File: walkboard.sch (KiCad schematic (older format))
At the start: 9 parts

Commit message: finished microcontroller
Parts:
- added C? (x2): 22pF, symbol Device:C_Small
- added F?: 500mA, symbol Device:Polyfuse_Small
- added J?: USB_C_Receptacle_USB2.0, symbol Connector:USB_C_Receptacle_USB2.0
- added R?: 10k, symbol Device:R_Small
- added SW?: SW_Push, symbol Switch:SW_Push
- added Y?: Crystal_GND24_Small, symbol Device:Crystal_GND24_Small
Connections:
- net labels added: D+, D-, VCC
- wire segments 25 -> 68

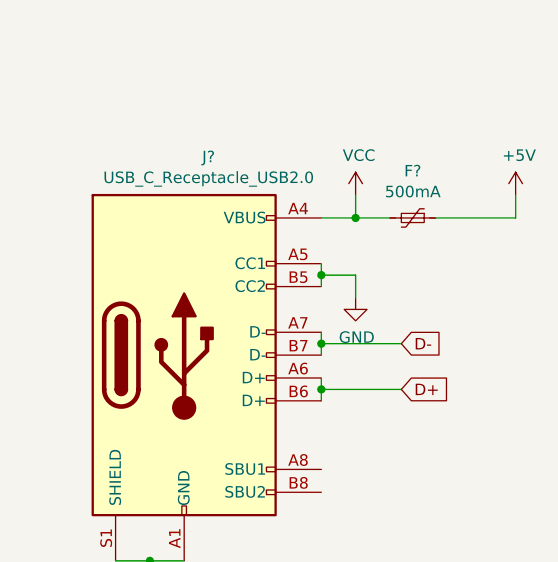
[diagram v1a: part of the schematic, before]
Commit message: added submodule for kaihl
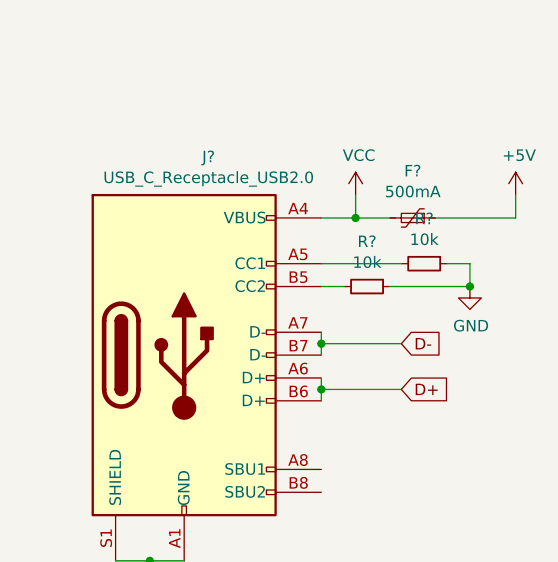
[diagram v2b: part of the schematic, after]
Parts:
- added R? (x2): 10k, symbol Device:R_Small
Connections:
- net GND: now also R?.1, R?.1; no longer J?.A5 (CC1), J?.B5 (CC2)
- new net: J?.B5 (CC2), R?.2
- new net: J?.A5 (CC1), R?.2
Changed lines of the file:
@@
 Text GLabel 7500 2100 2    50   Input ~ 0
 D-
-$Comp
-L power:GND #PWR?
-U 1 1 5F2C7BBD
-P 7300 1900
-F 0 "#PWR?" H 7300 1650 50  0001 C CNN
-F 1 "GND" H 7305 1727 50  0000 C CNN
-F 2 "" H 7300 1900 50  0001 C CNN
-F 3 "" H 7300 1900 50  0001 C CNN
-	1    7300 1900
-	1    0    0    -1
-$EndComp
-Wire Wire Line
-	7150 1750 7150 1800
-Wire Wire Line
-	7150 1800 7300 1800
-Wire Wire Line
-	7300 1800 7300 1900
-Connection ~ 7150 1800
-Wire Wire Line
-	7150 1800 7150 1850
 Wire Wire Line
 	7150 1550 7300 1550
@@
 Wire Wire Line
 	6400 3050 6550 3050
+$Comp
+L Device:R_Small R?
+U 1 1 5F2A1C28
+P 7350 1850
+F 0 "R?" V 7154 1850 50  0000 C CNN
+F 1 "10k" V 7245 1850 50  0000 C CNN
+F 2 "" H 7350 1850 50  0001 C CNN
+F 3 "~" H 7350 1850 50  0001 C CNN
+	1    7350 1850
+	0    1    1    0
+$EndComp
+$Comp
+L Device:R_Small R?
+U 1 1 5F2A2739
+P 7600 1750
+F 0 "R?" V 7404 1750 50  0000 C CNN
+F 1 "10k" V 7495 1750 50  0000 C CNN
+F 2 "" H 7600 1750 50  0001 C CNN
+F 3 "~" H 7600 1750 50  0001 C CNN
+	1    7600 1750
+	0    1    1    0
+$EndComp
+$Comp
+L power:GND #PWR?
+U 1 1 5F2A528D
+P 7800 1850
+F 0 "#PWR?" H 7800 1600 50  0001 C CNN
+F 1 "GND" H 7805 1677 50  0000 C CNN
+F 2 "" H 7800 1850 50  0001 C CNN
+F 3 "" H 7800 1850 50  0001 C CNN
+	1    7800 1850
+	1    0    0    -1
+$EndComp
+Wire Wire Line
+	7700 1750 7800 1750
+Wire Wire Line
+	7800 1750 7800 1850
+Wire Wire Line
+	7450 1850 7800 1850
+Connection ~ 7800 1850
+Wire Wire Line
+	7250 1850 7150 1850
+Wire Wire Line
+	7150 1750 7500 1750
 $EndSCHEMATC

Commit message: started work on pcb
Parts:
- removed R? (x2): 22, symbol Device:R_Small
- added D1, D10, D11, D12, D13, D14, D15, D16, D17, D18, D19, D2, D20, D21, D22, D23, D24, D25, D26, D27, D28, D29, D3, D30, D31, D32, D33, D34, D35, D36, D37, D38, D39, D4, D40, D41, D42, D43, D44, D45, D46, D47, D48, D49, D5, D50, D51, D52, D53, D54, D55, D56, D57, D58, D59, D6, D60, D61, D62, D63, D64, D65, D66, D67, D68, D7, D8, D9: D_Small, Diode_SMD:D_SOD-123, symbol Device:D_Small
- added MX1, MX10, MX11, MX12, MX13, MX14, MX15, MX16, MX17, MX18, MX19, MX2, MX20, MX21, MX22, MX23, MX24, MX25, MX26, MX27, MX28, MX29, MX3, MX30, MX31, MX32, MX33, MX34, MX35, MX36, MX37, MX38, MX39, MX4, MX40, MX41, MX42, MX43, MX44, MX45, MX46, MX47, MX48, MX49, MX5, MX50, MX51, MX52, MX53, MX54, MX55, MX56, MX57, MX58, MX59, MX6, MX60, MX61, MX62, MX63, MX64, MX65, MX66, MX67, MX7, MX8, MX9: MX-NoLED, keyswitches:Kailh_socket_MX, symbol MX_Alps_Hybrid:MX-NoLED
- added MX68: MX-NoLED, Resistor_SMD:R_0805_2012Metric, symbol MX_Alps_Hybrid:MX-NoLED
- added R2, R3: 22, Resistor_SMD:R_0612_1632Metric_Pad1.18x3.40mm_HandSolder, symbol Device:R_Small
- C1, C2, C3, C4, C5, C6: renamed from C?; footprint (none) -> Capacitor_SMD:C_0805_2012Metric_Pad1.15x1.40mm_HandSolder
- C7: renamed from C?; footprint (none) -> Diode_SMD:D_SOD-123
- F1: renamed from F?; footprint (none) -> keyswitches:Kailh_socket_MX
- J1: renamed from J?; footprint (none) -> Connector_USB:USB_C_Receptacle_HRO_TYPE-C-31-M-12
- R1, R4, R5, R6: renamed from R?; footprint (none) -> Resistor_SMD:R_0612_1632Metric_Pad1.18x3.40mm_HandSolder
- SW1: renamed from SW?; footprint (none) -> random-keyboard-parts:SKQG-1155865
- Y1: renamed from Y?; footprint (none) -> Crystal:Crystal_SMD_3225-4Pin_3.2x2.5mm
- gave numbers to parts that had none: 1
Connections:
- net D+: now also R2.2
- net D-: now also R3.2
- net at U1.3 (D-): now also R3.1
- net at U1.4 (D+): now also R2.1
- new net: D1.2 (A), MX1.2 (ROW)
- new net: D2.2 (A), MX2.2 (ROW)
- new net: D3.2 (A), MX3.2 (ROW)
- new net: D4.2 (A), MX4.2 (ROW)
- new net: D5.2 (A), MX5.2 (ROW)
- new net: D6.2 (A), MX6.2 (ROW)
- new net: D7.2 (A), MX7.2 (ROW)
- new net: D8.2 (A), MX8.2 (ROW)
- new net: D9.2 (A), MX9.2 (ROW)
- new net: D10.2 (A), MX10.2 (ROW)
- new net: D11.2 (A), MX11.2 (ROW)
- new net: D12.2 (A), MX12.2 (ROW)
- new net: D15.2 (A), MX15.2 (ROW)
- new net: D16.2 (A), MX16.2 (ROW)
- new net: D17.2 (A), MX17.2 (ROW)
- new net: D18.2 (A), MX18.2 (ROW)
- new net: D19.2 (A), MX19.2 (ROW)
- new net: D20.2 (A), MX20.2 (ROW)
- new net: D21.2 (A), MX21.2 (ROW)
- new net: D22.2 (A), MX22.2 (ROW)
- new net: D23.2 (A), MX23.2 (ROW)
- new net: D24.2 (A), MX24.2 (ROW)
- new net: D25.2 (A), MX25.2 (ROW)
- new net: D26.2 (A), MX26.2 (ROW)
- new net: D29.2 (A), MX29.2 (ROW)
- new net: D30.2 (A), MX30.2 (ROW)
- new net: D31.2 (A), MX31.2 (ROW)
- new net: D32.2 (A), MX32.2 (ROW)
- new net: D33.2 (A), MX33.2 (ROW)
- new net: D34.2 (A), MX34.2 (ROW)
- new net: D35.2 (A), MX35.2 (ROW)
- new net: D36.2 (A), MX36.2 (ROW)
- new net: D37.2 (A), MX37.2 (ROW)
- new net: D38.2 (A), MX38.2 (ROW)
- new net: D39.2 (A), MX39.2 (ROW)
- new net: D40.2 (A), MX40.2 (ROW)
- new net: D43.2 (A), MX43.2 (ROW)
- new net: D44.2 (A), MX44.2 (ROW)
- new net: D45.2 (A), MX45.2 (ROW)
- new net: D46.2 (A), MX46.2 (ROW)
- new net: D47.2 (A), MX47.2 (ROW)
- new net: D48.2 (A), MX48.2 (ROW)
- new net: D49.2 (A), MX49.2 (ROW)
- new net: D50.2 (A), MX50.2 (ROW)
- new net: D51.2 (A), MX51.2 (ROW)
- new net: D52.2 (A), MX52.2 (ROW)
- new net: D53.2 (A), MX53.2 (ROW)
- new net: D54.2 (A), MX54.2 (ROW)
- new net: D57.2 (A), MX57.2 (ROW)
- new net: D58.2 (A), MX58.2 (ROW)
- new net: D59.2 (A), MX59.2 (ROW)
- new net: D60.2 (A), MX60.2 (ROW)
- new net: D61.2 (A), MX61.2 (ROW)
- new net: D62.2 (A), MX62.2 (ROW)
- new net: D63.2 (A), MX63.2 (ROW)
- new net: D64.2 (A), MX64.2 (ROW)
- new net: D65.2 (A), MX65.2 (ROW)
- new net: D66.2 (A), MX66.2 (ROW)
- new net: D68.2 (A), MX68.2 (ROW)
- new net: D67.2 (A), MX67.2 (ROW)
- new net: D56.2 (A), MX56.2 (ROW)
- new net: D55.2 (A), MX55.2 (ROW)
- new net: D42.2 (A), MX42.2 (ROW)
- new net: D41.2 (A), MX41.2 (ROW)
- new net: D28.2 (A), MX28.2 (ROW)
- new net: D27.2 (A), MX27.2 (ROW)
- new net: D14.2 (A), MX14.2 (ROW)
- new net: D13.2 (A), MX13.2 (ROW)
- new net COL0: MX1.1 (COL), MX15.1 (COL), MX29.1 (COL), MX43.1 (COL), MX57.1 (COL)
- new net COL1: MX16.1 (COL), MX2.1 (COL), MX30.1 (COL), MX44.1 (COL), MX58.1 (COL)
- new net COL10: MX11.1 (COL), MX25.1 (COL), MX39.1 (COL), MX53.1 (COL), MX65.1 (COL)
- new net COL11: MX12.1 (COL), MX26.1 (COL), MX40.1 (COL), MX54.1 (COL), MX66.1 (COL)
- new net COL12: MX13.1 (COL), MX27.1 (COL), MX41.1 (COL), MX55.1 (COL), MX67.1 (COL)
- new net COL13: MX14.1 (COL), MX28.1 (COL), MX42.1 (COL), MX56.1 (COL), MX68.1 (COL)
- new net COL2: MX17.1 (COL), MX3.1 (COL), MX31.1 (COL), MX45.1 (COL), MX59.1 (COL)
- new net COL3: MX18.1 (COL), MX32.1 (COL), MX4.1 (COL), MX46.1 (COL), MX60.1 (COL)
- new net COL4: MX19.1 (COL), MX33.1 (COL), MX47.1 (COL), MX5.1 (COL), MX61.1 (COL)
- new net COL5: MX20.1 (COL), MX34.1 (COL), MX48.1 (COL), MX6.1 (COL), MX62.1 (COL)
- new net COL6: MX21.1 (COL), MX35.1 (COL), MX49.1 (COL), MX7.1 (COL)
- new net COL7: MX22.1 (COL), MX36.1 (COL), MX50.1 (COL), MX63.1 (COL), MX8.1 (COL)
- new net COL8: MX23.1 (COL), MX37.1 (COL), MX51.1 (COL), MX9.1 (COL)
- new net COL9: MX10.1 (COL), MX24.1 (COL), MX38.1 (COL), MX52.1 (COL), MX64.1 (COL)
- new net ROW0: D1.1 (K), D10.1 (K), D11.1 (K), D12.1 (K), D13.1 (K), D14.1 (K), D2.1 (K), D3.1 (K), D4.1 (K), D5.1 (K), D6.1 (K), D7.1 (K), D8.1 (K), D9.1 (K)
- new net ROW1: D15.1 (K), D16.1 (K), D17.1 (K), D18.1 (K), D19.1 (K), D20.1 (K), D21.1 (K), D22.1 (K), D23.1 (K), D24.1 (K), D25.1 (K), D26.1 (K), D27.1 (K), D28.1 (K)
- new net ROW2: D29.1 (K), D30.1 (K), D31.1 (K), D32.1 (K), D33.1 (K), D34.1 (K), D35.1 (K), D36.1 (K), D37.1 (K), D38.1 (K), D39.1 (K), D40.1 (K), D41.1 (K), D42.1 (K)
- new net ROW3: D43.1 (K), D44.1 (K), D45.1 (K), D46.1 (K), D47.1 (K), D48.1 (K), D49.1 (K), D50.1 (K), D51.1 (K), D52.1 (K), D53.1 (K), D54.1 (K), D55.1 (K), D56.1 (K)
- new net ROW4: D57.1 (K), D58.1 (K), D59.1 (K), D60.1 (K), D61.1 (K), D62.1 (K), D63.1 (K), D64.1 (K), D65.1 (K), D66.1 (K), D67.1 (K), D68.1 (K)
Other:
- moved on the sheet: F1, J1, R4, R5, R6

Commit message: fixed
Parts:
- added BT1: Battery_Cell, Connector_JST:JST_XH_S2B-XH-A_1x02_P2.50mm_Horizontal, symbol Device:Battery_Cell
- added C10: 4.7uF, Capacitor_SMD:C_0805_2012Metric_Pad1.15x1.40mm_HandSolder, symbol Device:C_Small
- added C11: 1uF, Capacitor_SMD:C_0805_2012Metric_Pad1.15x1.40mm_HandSolder, symbol Device:C_Small
- added C12: 22uF, Capacitor_SMD:C_0805_2012Metric_Pad1.15x1.40mm_HandSolder, symbol Device:C_Small
- added C8, C9: C_Small, Capacitor_SMD:C_0805_2012Metric_Pad1.15x1.40mm_HandSolder, symbol Device:C_Small
- added D69: D_Schottky, Diode_SMD:D_SOD-123, symbol Device:D_Schottky
- added L1: L_Small, Inductor_SMD:L_0805_2012Metric_Pad1.15x1.40mm_HandSolder, symbol Device:L_Small
- added Q1: Q_PMOS_DGS, Package_TO_SOT_SMD:SOT-23, symbol Device:Q_PMOS_DGS
- added R10, R8, R9: R_Small, Resistor_SMD:R_0805_2012Metric_Pad1.15x1.40mm_HandSolder, symbol Device:R_Small
- added R7: 10K, Resistor_SMD:R_0805_2012Metric_Pad1.15x1.40mm_HandSolder, symbol Device:R_Small
- added U2: MCP73831-2-OT, Package_TO_SOT_SMD:SOT-23-5, symbol Battery_Management:MCP73831-2-OT
- added U3: TPS61200DRC, Package_SON:Texas_S-PVSON-N10_ThermalVias, symbol Regulator_Switching:TPS61200DRC
- C7: value 0.1uF -> 10uF; footprint Diode_SMD:D_SOD-123 -> Capacitor_SMD:C_0805_2012Metric_Pad1.15x1.40mm_HandSolder
- F1: value 500mA -> Polyfuse_Small; footprint keyswitches:Kailh_socket_MX -> Fuse:Fuse_1206_3216Metric_Pad1.42x1.75mm_HandSolder
- MX68: footprint Resistor_SMD:R_0805_2012Metric -> keyswitches:Kailh_socket_MX
- R1, R2, R3, R4: footprint Resistor_SMD:R_0612_1632Metric_Pad1.18x3.40mm_HandSolder -> Resistor_SMD:R_0805_2012Metric_Pad1.15x1.40mm_HandSolder
- R5, R6: value 10k -> 5.1k; footprint Resistor_SMD:R_0612_1632Metric_Pad1.18x3.40mm_HandSolder -> Resistor_SMD:R_0805_2012Metric_Pad1.15x1.40mm_HandSolder
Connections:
- net +5V: now also C4.2, C5.2, C6.2, C7.2; no longer C4.1, C5.1, C6.1, C7.1, F1.1
- net GND: now also BT1.2 (-), C10.2, C11.2, C12.2, C8.2, C9.2, R10.2, R7.2, R8.2, U2.2 (VSS), U3.11 (PAD), U3.4 (PGND), U3.9 (GND); no longer C4.2, C5.2, C6.2, C7.2
- net VCC: no longer names the net of J1.A4 (VBUS), J1.A9 (VBUS), J1.B4 (VBUS), J1.B9 (VBUS)
- net VCC: now also F1.1; no longer F1.2
- new net: C11.1, U3.1 (VAUX)
- new net: C12.1, C4.1, C5.1, C6.1, C7.1, D69.1 (K), U3.10 (FB), U3.2 (VOUT)
- new net: L1.2, U3.3 (L)
- new net: C10.1, L1.1, Q1.1 (D), R9.1, U3.5 (VIN), U3.6 (EN), U3.8 (PS)
- new net: R10.1, R9.2, U3.7 (UVLO)
- new net: BT1.1 (+), C9.1, Q1.3 (S), U2.3 (VBAT)
- new net: C8.1, D69.2 (A), F1.2, Q1.2 (G), R7.1, U2.4 (VDD)
- new net: R8.1, U2.5 (PROG)
- no-connect marks 0 -> 3
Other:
- moved on the sheet: C1, C2, C3, D1, D10, D11, D12, D13, D14, D15, D16, D17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
